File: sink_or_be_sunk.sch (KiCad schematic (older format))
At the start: 79 parts, among them J1 Grid_Conn, J10 640456-2, J10 Grid_Conn, J11 Grid_Conn, J12 Grid_Conn, J13 Grid_Conn, J14 Grid_Conn, J15 Grid_Conn, J16 Grid_Conn, J17 USB_B_Micro, J18 Keypad_Conn, J19 Display_Conn, J2 640456-6, J20 JTAG_Conn, J21 Debug_Conn, J22 Battery_Conn, J3 640456-6, J4 640456-6, J5 640456-6, J6 640456-6, J7 640456-6, J8 640456-6, J9 640456-2, J9 Grid_Conn, M1 Motor_DC, Q1 IRL530, Q2 Q_PMOS_GDS, Q3 2N3704, Q4 2N3704, SW1 SW_DPST, SW2 Reset_SW, U1 SN74HC151N, U2 SwitchingRegulator, U3 MCP73831-2-OT, U4 MCP608, U5 ESP32-WROOM-32, U6 CY7C65213A-28PVXI

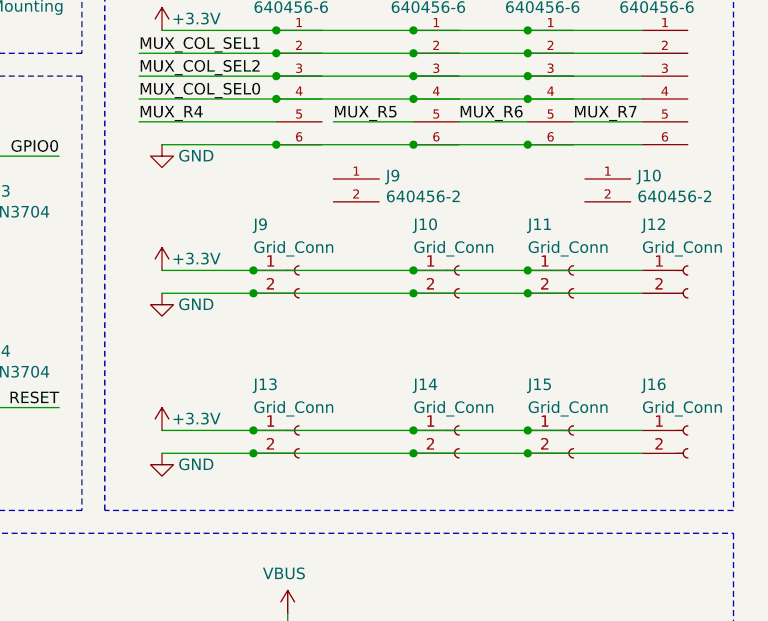
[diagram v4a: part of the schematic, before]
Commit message: brought over board from regulator
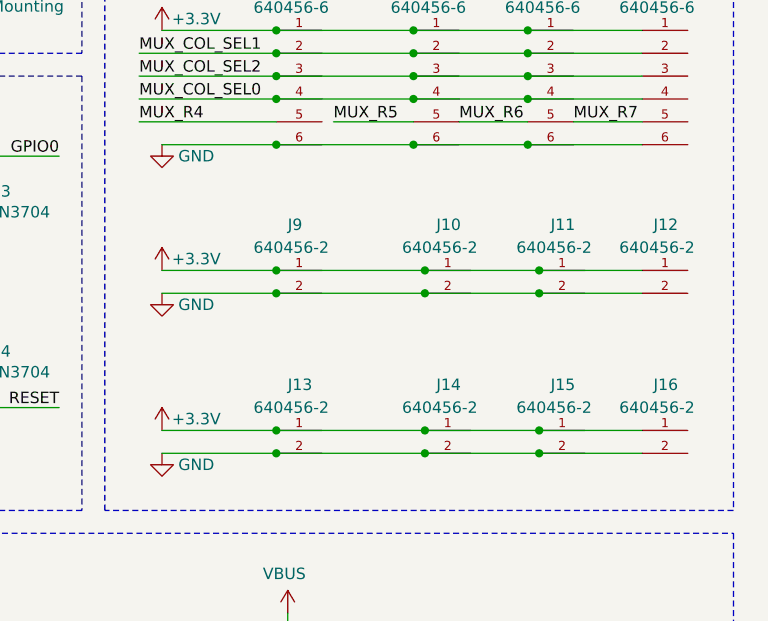
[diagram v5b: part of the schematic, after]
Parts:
- removed J10, J11, J12, J13, J14, J15, J16, J9: Grid_Conn, JST_Conn:TE_640456-2, symbol Connector:Conn_01x02_Female
- added J11, J12, J13, J14, J15, J16: 640456-2, JST_Conn:TE_640456-2, symbol JST_Conn:640456-2
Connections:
- net +3V3: now also J10.1, J9.1, J11.1, J12.1, J13.1, J14.1, J15.1, J16.1
- net GND: now also J10.2, J9.2, J11.2, J12.2, J13.2, J14.2, J15.2, J16.2
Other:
- moved on the sheet: J10, J9
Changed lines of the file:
@@
 	10800 2250 10500 2250
-$Comp
-L Connector:Conn_01x02_Female J9
-U 1 1 61CE250A
-P 9300 2900
-F 0 "J9" H 9100 3100 50  0000 L CNN
-F 1 "Grid_Conn" H 9100 3000 50  0000 L CNN
-F 2 "JST_Conn:TE_640456-2" H 9300 2900 50  0001 C CNN
-F 3 "~" H 9300 2900 50  0001 C CNN
-	1    9300 2900
-	1    0    0    -1
-$EndComp
-Wire Wire Line
-	9100 2900 8700 2900
-Wire Wire Line
-	9100 3000 8700 3000
-$Comp
-L Connector:Conn_01x02_Female J10
-U 1 1 61EE3CE7
-P 10000 2900
-F 0 "J10" H 9800 3100 50  0000 L CNN
-F 1 "Grid_Conn" H 9800 3000 50  0000 L CNN
-F 2 "JST_Conn:TE_640456-2" H 10000 2900 50  0001 C CNN
-F 3 "~" H 10000 2900 50  0001 C CNN
-	1    10000 2900
-	1    0    0    -1
-$EndComp
-$Comp
-L Connector:Conn_01x02_Female J11
-U 1 1 61F00D33
-P 10500 2900
-F 0 "J11" H 10300 3100 50  0000 L CNN
-F 1 "Grid_Conn" H 10300 3000 50  0000 L CNN
-F 2 "JST_Conn:TE_640456-2" H 10500 2900 50  0001 C CNN
-F 3 "~" H 10500 2900 50  0001 C CNN
-	1    10500 2900
-	1    0    0    -1
-$EndComp
-$Comp
-L Connector:Conn_01x02_Female J12
-U 1 1 61F1D68F
-P 11000 2900
-F 0 "J12" H 10800 3100 50  0000 L CNN
-F 1 "Grid_Conn" H 10800 3000 50  0000 L CNN
-F 2 "JST_Conn:TE_640456-2" H 11000 2900 50  0001 C CNN
-F 3 "~" H 11000 2900 50  0001 C CNN
-	1    11000 2900
-	1    0    0    -1
-$EndComp
-Wire Wire Line
-	9100 2900 9800 2900
-Connection ~ 9100 2900
-Connection ~ 9800 2900
-Wire Wire Line
-	9800 2900 10300 2900
-Connection ~ 10300 2900
-Wire Wire Line
-	10300 2900 10800 2900
-Wire Wire Line
-	10800 3000 10300 3000
-Connection ~ 9100 3000
-Connection ~ 9800 3000
-Wire Wire Line
-	9800 3000 9100 3000
-Connection ~ 10300 3000
-Wire Wire Line
-	10300 3000 9800 3000
 $Comp
 L power:+3.3V #PWR043
@@
 	1    0    0    -1
 $EndComp
-$Comp
-L Connector:Conn_01x02_Female J13
-U 1 1 61FD13D4
-P 9300 3600
-F 0 "J13" H 9100 3800 50  0000 L CNN
-F 1 "Grid_Conn" H 9100 3700 50  0000 L CNN
-F 2 "JST_Conn:TE_640456-2" H 9300 3600 50  0001 C CNN
-F 3 "~" H 9300 3600 50  0001 C CNN
-	1    9300 3600
-	1    0    0    -1
-$EndComp
-Wire Wire Line
-	9100 3600 8700 3600
-Wire Wire Line
-	9100 3700 8700 3700
-$Comp
-L Connector:Conn_01x02_Female J14
-U 1 1 61FD13DC
-P 10000 3600
-F 0 "J14" H 9800 3800 50  0000 L CNN
-F 1 "Grid_Conn" H 9800 3700 50  0000 L CNN
-F 2 "JST_Conn:TE_640456-2" H 10000 3600 50  0001 C CNN
-F 3 "~" H 10000 3600 50  0001 C CNN
-	1    10000 3600
-	1    0    0    -1
-$EndComp
-$Comp
-L Connector:Conn_01x02_Female J15
-U 1 1 61FD13E2
-P 10500 3600
-F 0 "J15" H 10300 3800 50  0000 L CNN
-F 1 "Grid_Conn" H 10300 3700 50  0000 L CNN
-F 2 "JST_Conn:TE_640456-2" H 10500 3600 50  0001 C CNN
-F 3 "~" H 10500 3600 50  0001 C CNN
-	1    10500 3600
-	1    0    0    -1
-$EndComp
-$Comp
-L Connector:Conn_01x02_Female J16
-U 1 1 61FD13E8
-P 11000 3600
-F 0 "J16" H 10800 3800 50  0000 L CNN
-F 1 "Grid_Conn" H 10800 3700 50  0000 L CNN
-F 2 "JST_Conn:TE_640456-2" H 11000 3600 50  0001 C CNN
-F 3 "~" H 11000 3600 50  0001 C CNN
-	1    11000 3600
-	1    0    0    -1
-$EndComp
-Wire Wire Line
-	9100 3600 9800 3600
-Connection ~ 9100 3600
-Connection ~ 9800 3600
-Wire Wire Line
-	9800 3600 10300 3600
-Connection ~ 10300 3600
-Wire Wire Line
-	10300 3600 10800 3600
-Wire Wire Line
-	10800 3700 10300 3700
-Connection ~ 9100 3700
-Connection ~ 9800 3700
-Wire Wire Line
-	9800 3700 9100 3700
-Connection ~ 10300 3700
-Wire Wire Line
-	10300 3700 9800 3700
 Text Label 850  6350 0    50   ~ 0
 MUX_R5
@@
 	10300 2350 10800 2350
 $Comp
+L JST_Conn:640456-2 J10
+U 1 1 61BA241D
+P 9950 3000
+F 0 "J10" H 9900 3300 50  0000 L CNN
+F 1 "640456-2" H 9750 3200 50  0000 L CNN
+F 2 "JST_Conn:TE_640456-2" H 9750 2900 50  0001 L BNN
+F 3 "" H 9950 3000 50  0001 L BNN
+	1    9950 3000
+	1    0    0    -1
+$EndComp
+$Comp
+L JST_Conn:640456-2 J11
+U 1 1 61BA36C6
+P 10450 3000
+F 0 "J11" H 10400 3300 50  0000 L CNN
+F 1 "640456-2" H 10250 3200 50  0000 L CNN
+F 2 "JST_Conn:TE_640456-2" H 10250 2900 50  0001 L BNN
+F 3 "" H 10450 3000 50  0001 L BNN
+	1    10450 3000
+	1    0    0    -1
+$EndComp
+$Comp
+L JST_Conn:640456-2 J12
+U 1 1 61BA3965
+P 10900 3000
+F 0 "J12" H 10850 3300 50  0000 L CNN
+F 1 "640456-2" H 10700 3200 50  0000 L CNN
+F 2 "JST_Conn:TE_640456-2" H 10700 2900 50  0001 L BNN
+F 3 "" H 10900 3000 50  0001 L BNN
+	1    10900 3000
+	1    0    0    -1
+$EndComp
+Wire Wire Line
+	8700 3000 9200 3000
+Wire Wire Line
+	8700 2900 9200 2900
+$Comp
 L JST_Conn:640456-2 J9
 U 1 1 61BA1C7E
-P 9550 2600
-F 0 "J9" H 9679 2713 50  0000 L CNN
-F 1 "640456-2" H 9679 2622 50  0000 L CNN
-F 2 "JST_Conn:TE_640456-2" H 9350 2500 50  0001 L BNN
-F 3 "" H 9550 2600 50  0001 L BNN
-	1    9550 2600
-	1    0    0    -1
-$EndComp
-$Comp
-L JST_Conn:640456-2 J10
-U 1 1 61BA241D
-P 10650 2600
-F 0 "J10" H 10779 2713 50  0000 L CNN
-F 1 "640456-2" H 10779 2622 50  0000 L CNN
-F 2 "JST_Conn:TE_640456-2" H 10450 2500 50  0001 L BNN
-F 3 "" H 10650 2600 50  0001 L BNN
-	1    10650 2600
-	1    0    0    -1
-$EndComp
+P 9300 3000
+F 0 "J9" H 9250 3300 50  0000 L CNN
+F 1 "640456-2" H 9100 3200 50  0000 L CNN
+F 2 "JST_Conn:TE_640456-2" H 9100 2900 50  0001 L BNN
+F 3 "" H 9300 3000 50  0001 L BNN
+	1    9300 3000
+	1    0    0    -1
+$EndComp
+Connection ~ 9200 2900
+Connection ~ 9200 3000
+Wire Wire Line
+	9200 2900 9850 2900
+Wire Wire Line
+	9200 3000 9850 3000
+Connection ~ 9850 2900
+Connection ~ 9850 3000
+Wire Wire Line
+	9850 2900 10350 2900
+Wire Wire Line
+	9850 3000 10350 3000
+Connection ~ 10350 2900
+Wire Wire Line
+	10350 2900 10800 2900
+Connection ~ 10350 3000
+Wire Wire Line
+	10350 3000 10800 3000
+$Comp
+L JST_Conn:640456-2 J13
+U 1 1 61BA719A
+P 9300 3700
+F 0 "J13" H 9250 4000 50  0000 L CNN
+F 1 "640456-2" H 9100 3900 50  0000 L CNN
+F 2 "JST_Conn:TE_640456-2" H 9100 3600 50  0001 L BNN
+F 3 "" H 9300 3700 50  0001 L BNN
+	1    9300 3700
+	1    0    0    -1
+$EndComp
+$Comp
+L JST_Conn:640456-2 J14
+U 1 1 61BA7D8F
+P 9950 3700
+F 0 "J14" H 9900 4000 50  0000 L CNN
+F 1 "640456-2" H 9750 3900 50  0000 L CNN
+F 2 "JST_Conn:TE_640456-2" H 9750 3600 50  0001 L BNN
+F 3 "" H 9950 3700 50  0001 L BNN
+	1    9950 3700
+	1    0    0    -1
+$EndComp
+$Comp
+L JST_Conn:640456-2 J15
+U 1 1 61BA8593
+P 10450 3700
+F 0 "J15" H 10400 4000 50  0000 L CNN
+F 1 "640456-2" H 10250 3900 50  0000 L CNN
+F 2 "JST_Conn:TE_640456-2" H 10250 3600 50  0001 L BNN
+F 3 "" H 10450 3700 50  0001 L BNN
+	1    10450 3700
+	1    0    0    -1
+$EndComp
+$Comp
+L JST_Conn:640456-2 J16
+U 1 1 61BA87B1
+P 10900 3700
+F 0 "J16" H 10850 4000 50  0000 L CNN
+F 1 "640456-2" H 10700 3900 50  0000 L CNN
+F 2 "JST_Conn:TE_640456-2" H 10700 3600 50  0001 L BNN
+F 3 "" H 10900 3700 50  0001 L BNN
+	1    10900 3700
+	1    0    0    -1
+$EndComp
+Wire Wire Line
+	8700 3600 9200 3600
+Connection ~ 9200 3600
+Wire Wire Line
+	9200 3600 9850 3600
+Connection ~ 9850 3600
+Wire Wire Line
+	9850 3600 10350 3600
+Connection ~ 10350 3600
+Wire Wire Line
+	10350 3600 10800 3600
+Wire Wire Line
+	10800 3700 10350 3700
+Connection ~ 9200 3700
+Wire Wire Line
+	9200 3700 8700 3700
+Connection ~ 9850 3700
+Wire Wire Line
+	9850 3700 9200 3700
+Connection ~ 10350 3700
+Wire Wire Line
+	10350 3700 9850 3700
 $EndSCHEMATC

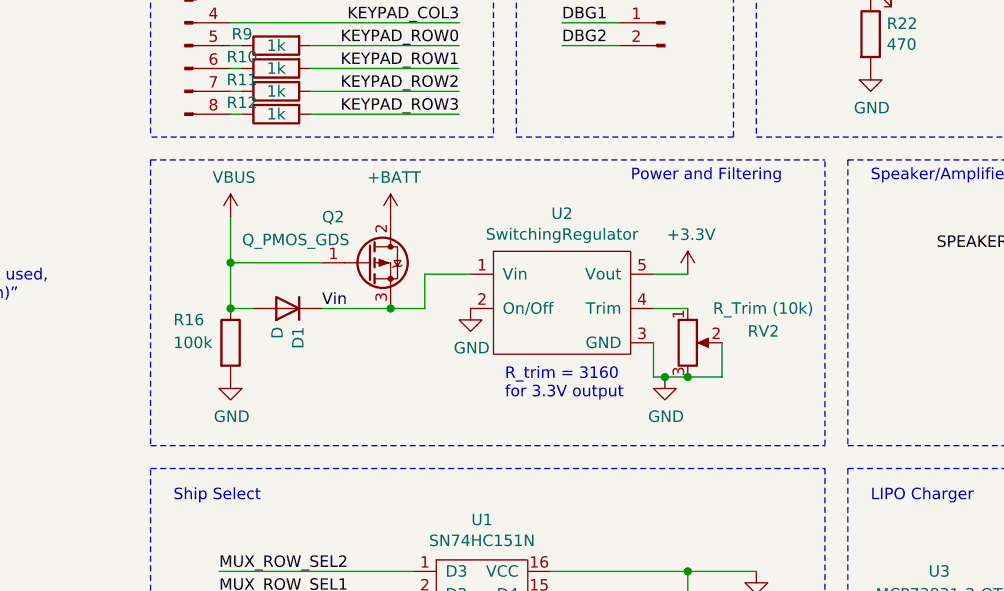
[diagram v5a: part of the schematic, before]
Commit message: updated with new regulator symbol
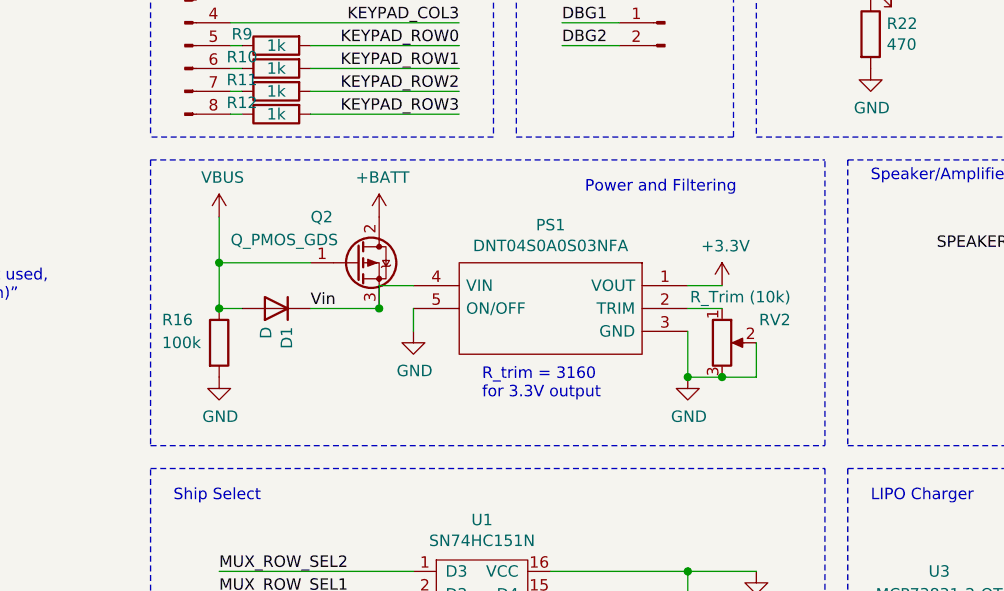
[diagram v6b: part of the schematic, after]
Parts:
- removed U2: SwitchingRegulator, PCB_ESP32:SwitchingRegulator, symbol esp_board:SwitchingRegulator
- added PS1: DNT04S0A0S03NFA, DNT04S0A0S03NFA, symbol esp_board:DNT04S0A0S03NFA
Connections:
- net +3V3: now also PS1.1 (VOUT)
- net GND: now also PS1.3 (GND), PS1.5 (ON/OFF)
- net Vin: now also PS1.4 (VIN)
- net at RV2.1: now also PS1.2 (TRIM)
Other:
- moved on the sheet: D1, Q2, R16, RV2
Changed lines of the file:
@@
 Text Notes 650  5550 0    50   ~ 0
 Ship Select
-Text Notes 2650 4150 0    50   ~ 0
-Power and Filtering
 $Comp
 L power:VBUS #PWR015
@@
 L power:+BATT #PWR014
 U 1 1 61C44AB1
-P 1600 4300
-F 0 "#PWR014" H 1600 4150 50  0001 C CNN
-F 1 "+BATT" H 1615 4473 50  0000 C CNN
-F 2 "" H 1600 4300 50  0001 C CNN
-F 3 "" H 1600 4300 50  0001 C CNN
-	1    1600 4300
+P 1550 4300
+F 0 "#PWR014" H 1550 4150 50  0001 C CNN
+F 1 "+BATT" H 1565 4473 50  0000 C CNN
+F 2 "" H 1550 4300 50  0001 C CNN
+F 3 "" H 1550 4300 50  0001 C CNN
+	1    1550 4300
 	1    0    0    -1
 $EndComp
@@
 L Device:R R16
 U 1 1 61B8EE7E
-P 900 4850
-F 0 "R16" H 650 4950 50  0000 L CNN
-F 1 "100k" H 650 4850 50  0000 L CNN
-F 2 "Resistor_SMD:R_0805_2012Metric_Pad1.15x1.40mm_HandSolder" V 830 4850 50  0001 C CNN
-F 3 "~" H 900 4850 50  0001 C CNN
-	1    900  4850
+P 850 4850
+F 0 "R16" H 600 4950 50  0000 L CNN
+F 1 "100k" H 600 4850 50  0000 L CNN
+F 2 "Resistor_SMD:R_0805_2012Metric_Pad1.15x1.40mm_HandSolder" V 780 4850 50  0001 C CNN
+F 3 "~" H 850 4850 50  0001 C CNN
+	1    850  4850
 	1    0    0    -1
 $EndComp
@@
 L power:VBUS #PWR06
 U 1 1 616721DB
-P 900 4300
-F 0 "#PWR06" H 900 4150 50  0001 C CNN
-F 1 "VBUS" H 915 4473 50  0000 C CNN
-F 2 "" H 900 4300 50  0001 C CNN
-F 3 "" H 900 4300 50  0001 C CNN
-	1    900  4300
-	1    0    0    -1
-$EndComp
-Wire Wire Line
-	900  4300 900  4500
-Wire Wire Line
-	900  4700 1000 4700
-Connection ~ 900  4700
+P 850 4300
+F 0 "#PWR06" H 850 4150 50  0001 C CNN
+F 1 "VBUS" H 865 4473 50  0000 C CNN
+F 2 "" H 850 4300 50  0001 C CNN
+F 3 "" H 850 4300 50  0001 C CNN
+	1    850  4300
+	1    0    0    -1
+$EndComp
+Wire Wire Line
+	850  4300 850  4500
+Wire Wire Line
+	850  4700 950  4700
+Connection ~ 850  4700
 $Comp
 L power:GND #PWR07
 U 1 1 61C53673
-P 900 5000
-F 0 "#PWR07" H 900 4750 50  0001 C CNN
-F 1 "GND" H 905 4827 50  0000 C CNN
-F 2 "" H 900 5000 50  0001 C CNN
-F 3 "" H 900 5000 50  0001 C CNN
-	1    900  5000
-	1    0    0    -1
-$EndComp
-Wire Wire Line
-	1300 4500 900  4500
-Connection ~ 900  4500
-Wire Wire Line
-	900  4500 900  4700
+P 850 5000
+F 0 "#PWR07" H 850 4750 50  0001 C CNN
+F 1 "GND" H 855 4827 50  0000 C CNN
+F 2 "" H 850 5000 50  0001 C CNN
+F 3 "" H 850 5000 50  0001 C CNN
+	1    850  5000
+	1    0    0    -1
+$EndComp
+Wire Wire Line
+	1250 4500 850  4500
+Connection ~ 850  4500
+Wire Wire Line
+	850  4500 850  4700
 $Comp
 L Device:D D1
 U 1 1 61CAFF58
-P 1150 4700
-F 0 "D1" V 1104 4780 50  0000 L CNN
-F 1 "D" V 1195 4780 50  0000 L CNN
-F 2 "Diode_THT:D_A-405_P7.62mm_Horizontal" H 1150 4700 50  0001 C CNN
-F 3 "https://www.onsemi.com/pdf/datasheet/1n5817-d.pdf" H 1150 4700 50  0001 C CNN
-	1    1150 4700
+P 1100 4700
+F 0 "D1" V 1054 4780 50  0000 L CNN
+F 1 "D" V 1145 4780 50  0000 L CNN
+F 2 "Diode_THT:D_A-405_P7.62mm_Horizontal" H 1100 4700 50  0001 C CNN
+F 3 "https://www.onsemi.com/pdf/datasheet/1n5817-d.pdf" H 1100 4700 50  0001 C CNN
+	1    1100 4700
 	-1   0    0    1
 $EndComp
-Text Label 1300 4700 0    50   ~ 0
+Text Label 1250 4700 0    50   ~ 0
 Vin
 Wire Wire Line
-	1600 4700 1300 4700
+	1550 4700 1250 4700
 $Comp
 L Device:Q_PMOS_GDS Q2
 U 1 1 61B8D24F
-P 1500 4500
-F 0 "Q2" H 1300 4700 50  0000 L CNN
-F 1 "Q_PMOS_GDS" H 950 4600 50  0000 L CNN
-F 2 "Package_TO_SOT_THT:TO-251-3-1EP_Horizontal_TabDown" H 1700 4600 50  0001 C CNN
-F 3 "https://rocelec.widen.net/view/pdf/6e63ma1bli/ONSM-S-A0003587829-1.pdf?t.download=true&u=5oefqw~" H 1500 4500 50  0001 C CNN
-	1    1500 4500
+P 1450 4500
+F 0 "Q2" H 1250 4700 50  0000 L CNN
+F 1 "Q_PMOS_GDS" H 900 4600 50  0000 L CNN
+F 2 "Package_TO_SOT_THT:TO-251-3-1EP_Horizontal_TabDown" H 1650 4600 50  0001 C CNN
+F 3 "https://rocelec.widen.net/view/pdf/6e63ma1bli/ONSM-S-A0003587829-1.pdf?t.download=true&u=5oefqw~" H 1450 4500 50  0001 C CNN
+	1    1450 4500
 	1    0    0    -1
 $EndComp
@@
 Wire Notes Line
 	550  2800 3100 2800
-$Comp
-L Device:R_POT RV2
-U 1 1 616E74CB
-P 2900 4850
-F 0 "RV2" H 3300 4900 50  0000 R CNN
-F 1 "R_Trim (10k)" H 3450 5000 50  0000 R CNN
-F 2 "Potentiometer_THT:Potentiometer_Bourns_3266Y_Vertical" H 2900 4850 50  0001 C CNN
-F 3 "~" H 2900 4850 50  0001 C CNN
-	1    2900 4850
-	1    0    0    -1
-$EndComp
-$Comp
-L power:GND #PWR02
-U 1 1 617355CE
-P 1950 4700
-F 0 "#PWR02" H 1950 4450 50  0001 C CNN
-F 1 "GND" H 1955 4527 50  0000 C CNN
-F 2 "" H 1950 4700 50  0001 C CNN
-F 3 "" H 1950 4700 50  0001 C CNN
-	1    1950 4700
-	1    0    0    -1
-$EndComp
 Text Notes -1400 4750 0    50   ~ 0
 “If the negative On/Off function is not used, \ntie the pin to GND. (module will be On)”\n(datasheet pg.8 above Figure 26)
-Wire Wire Line
-	2750 4850 2750 5000
-$Comp
-L power:GND #PWR03
-U 1 1 6173594A
-P 2800 5000
-F 0 "#PWR03" H 2800 4750 50  0001 C CNN
-F 1 "GND" H 2805 4827 50  0000 C CNN
-F 2 "" H 2800 5000 50  0001 C CNN
-F 3 "" H 2800 5000 50  0001 C CNN
-	1    2800 5000
-	1    0    0    -1
-$EndComp
-Wire Wire Line
-	2750 4700 2900 4700
-Wire Wire Line
-	2900 5000 2800 5000
-Connection ~ 2800 5000
-Wire Wire Line
-	2800 5000 2750 5000
-Wire Wire Line
-	3050 4850 3050 5000
-Wire Wire Line
-	3050 5000 2900 5000
-Connection ~ 2900 5000
-Text Notes 2100 5100 0    50   ~ 0
+Text Notes 2000 5100 0    50   ~ 0
 R_trim = 3160\nfor 3.3V output
-$Comp
-L power:+3.3V #PWR017
-U 1 1 61719CD4
-P 2900 4550
-F 0 "#PWR017" H 2900 4400 50  0001 C CNN
-F 1 "+3.3V" H 2915 4723 50  0000 C CNN
-F 2 "" H 2900 4550 50  0001 C CNN
-F 3 "" H 2900 4550 50  0001 C CNN
-	1    2900 4550
-	1    0    0    -1
-$EndComp
-Wire Wire Line
-	2750 4550 2900 4550
-Wire Wire Line
-	1750 4700 1600 4700
-Connection ~ 1600 4700
-Wire Wire Line
-	1950 4550 1750 4550
-Wire Wire Line
-	1750 4550 1750 4700
 $Comp
 L Connector:USB_B_Micro J17
@@
 	1    0    0    -1
 $EndComp
-$Comp
-L esp_board:SwitchingRegulator U2
-U 1 1 61A086E5
-P 2400 4800
-F 0 "U2" H 2350 5315 50  0000 C CNN
-F 1 "SwitchingRegulator" H 2350 5224 50  0000 C CNN
-F 2 "PCB_ESP32:SwitchingRegulator" H 2400 4800 50  0001 C CNN
-F 3 "" H 2400 4800 50  0001 C CNN
-	1    2400 4800
-	1    0    0    -1
-$EndComp
 Wire Wire Line
 	8700 1350 9200 1350
@@
 Wire Wire Line
 	10350 3700 9850 3700
+Wire Wire Line
+	2900 4600 3050 4600
+$Comp
+L power:+3.3V #PWR017
+U 1 1 61719CD4
+P 3050 4600
+F 0 "#PWR017" H 3050 4450 50  0001 C CNN
+F 1 "+3.3V" H 3065 4773 50  0000 C CNN
+F 2 "" H 3050 4600 50  0001 C CNN
+F 3 "" H 3050 4600 50  0001 C CNN
+	1    3050 4600
+	1    0    0    -1
+$EndComp
+$Comp
+L power:GND #PWR03
+U 1 1 6173594A
+P 2900 5000
+F 0 "#PWR03" H 2900 4750 50  0001 C CNN
+F 1 "GND" H 2905 4827 50  0000 C CNN
+F 2 "" H 2900 5000 50  0001 C CNN
+F 3 "" H 2900 5000 50  0001 C CNN
+	1    2900 5000
+	1    0    0    -1
+$EndComp
+Text Notes 2450 4200 0    50   ~ 0
+Power and Filtering
+$Comp
+L power:GND #PWR02
+U 1 1 617355CE
+P 1700 4800
+F 0 "#PWR02" H 1700 4550 50  0001 C CNN
+F 1 "GND" H 1705 4627 50  0000 C CNN
+F 2 "" H 1700 4800 50  0001 C CNN
+F 3 "" H 1700 4800 50  0001 C CNN
+	1    1700 4800
+	1    0    0    -1
+$EndComp
+Wire Wire Line
+	2900 4700 3050 4700
+$Comp
+L Device:R_POT RV2
+U 1 1 616E74CB
+P 3050 4850
+F 0 "RV2" H 3350 4950 50  0000 R CNN
+F 1 "R_Trim (10k)" H 3350 5050 50  0000 R CNN
+F 2 "Potentiometer_THT:Potentiometer_Bourns_3266Y_Vertical" H 3050 4850 50  0001 C CNN
+F 3 "~" H 3050 4850 50  0001 C CNN
+	1    3050 4850
+	1    0    0    -1
+$EndComp
+Wire Wire Line
+	3200 4850 3200 5000
+Wire Wire Line
+	3200 5000 3050 5000
+Connection ~ 3050 5000
+Wire Wire Line
+	2900 4800 2900 5000
+Connection ~ 2900 5000
+Wire Wire Line
+	2900 5000 3050 5000
+$Comp
+L esp_board:DNT04S0A0S03NFA PS1
+U 1 1 61CAEF4C
+P 2900 4600
+F 0 "PS1" H 3500 4865 50  0000 C CNN
+F 1 "DNT04S0A0S03NFA" H 3500 4774 50  0000 C CNN
+F 2 "DNT04S0A0S03NFA" H 3950 4700 50  0001 L CNN
+F 3 "https://componentsearchengine.com/Datasheets/1/DNT04S0A0S03NFA.pdf" H 3950 4600 50  0001 L CNN
+F 4 "Non-Isolated DC/DC Converters DOSA POL I DC/DC Module, 3A" H 3950 4500 50  0001 L CNN "Description"
+F 5 "6.9" H 3950 4400 50  0001 L CNN "Height"
+F 6 "108-DNT04S0A0S03NFA" H 3950 4300 50  0001 L CNN "Mouser Part Number"
+F 7 "https://www.mouser.com/Search/Refine.aspx?Keyword=108-DNT04S0A0S03NFA" H 3950 4200 50  0001 L CNN "Mouser Price/Stock"
+F 8 "Delta Electronics" H 3950 4100 50  0001 L CNN "Manufacturer_Name"
+F 9 "DNT04S0A0S03NFA" H 3950 4000 50  0001 L CNN "Manufacturer_Part_Number"
+	1    2900 4600
+	-1   0    0    -1
+$EndComp
+Wire Wire Line
+	1700 4600 1550 4600
+Wire Wire Line
+	1550 4600 1550 4700
+Connection ~ 1550 4700
+Wire Wire Line
+	1700 4700 1700 4800
 $EndSCHEMATC

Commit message: brought over regulator footprint
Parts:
- PS1: footprint DNT04S0A0S03NFA -> PCB_ESP32:DNT04S0A0S03NFA
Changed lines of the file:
@@
 F 0 "PS1" H 3500 4865 50  0000 C CNN
 F 1 "DNT04S0A0S03NFA" H 3500 4774 50  0000 C CNN
-F 2 "DNT04S0A0S03NFA" H 3950 4700 50  0001 L CNN
+F 2 "PCB_ESP32:DNT04S0A0S03NFA" H 3950 4700 50  0001 L CNN
 F 3 "https://componentsearchengine.com/Datasheets/1/DNT04S0A0S03NFA.pdf" H 3950 4600 50  0001 L CNN
 F 4 "Non-Isolated DC/DC Converters DOSA POL I DC/DC Module, 3A" H 3950 4500 50  0001 L CNN "Description"
